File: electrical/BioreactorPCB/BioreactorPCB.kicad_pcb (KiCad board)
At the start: 2 copper layers, 90.7 x 84.9 mm, 90 parts, among them IC1 AL5809-20P1-7, IC2 VEML7700-TR, J1 61300311121, J10 USB_B, J11 Conn_01x06_Male, J12 Conn_02x03_Odd_Even, J13 PJ-202A, J14 Conn_01x05_Male, J15 Conn_01x06_Male, J16 Conn_01x06_Male, J2 61300311121, J3 Conn_01x05_Male, J4 Conn_01x06_Male, J5 OSTTC022162, J6 OSTTC022162, J7 OSTTC042162, J8 OSTTC042162, J9 OSTTC042162, Q1 2N3905, Q2 IRF540N, Q3 FQP47P06, Q4 TL2575HV-05IKV, U1 L293D, U2 FT232RL, U3 ATMEGA328P-AUR, U4 TCA39306DCUR, U5 ATmega328PB-M, Y1 16 mHz

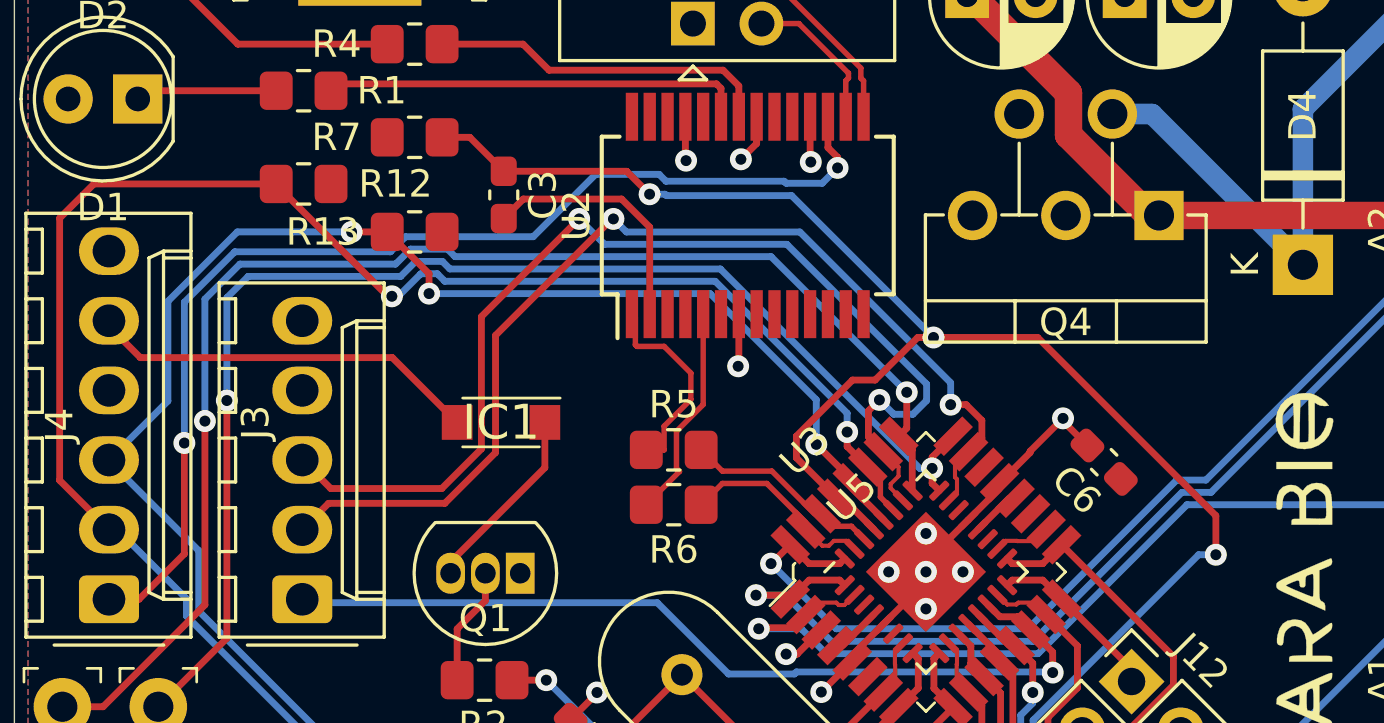
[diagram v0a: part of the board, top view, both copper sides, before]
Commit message: some track cleanup
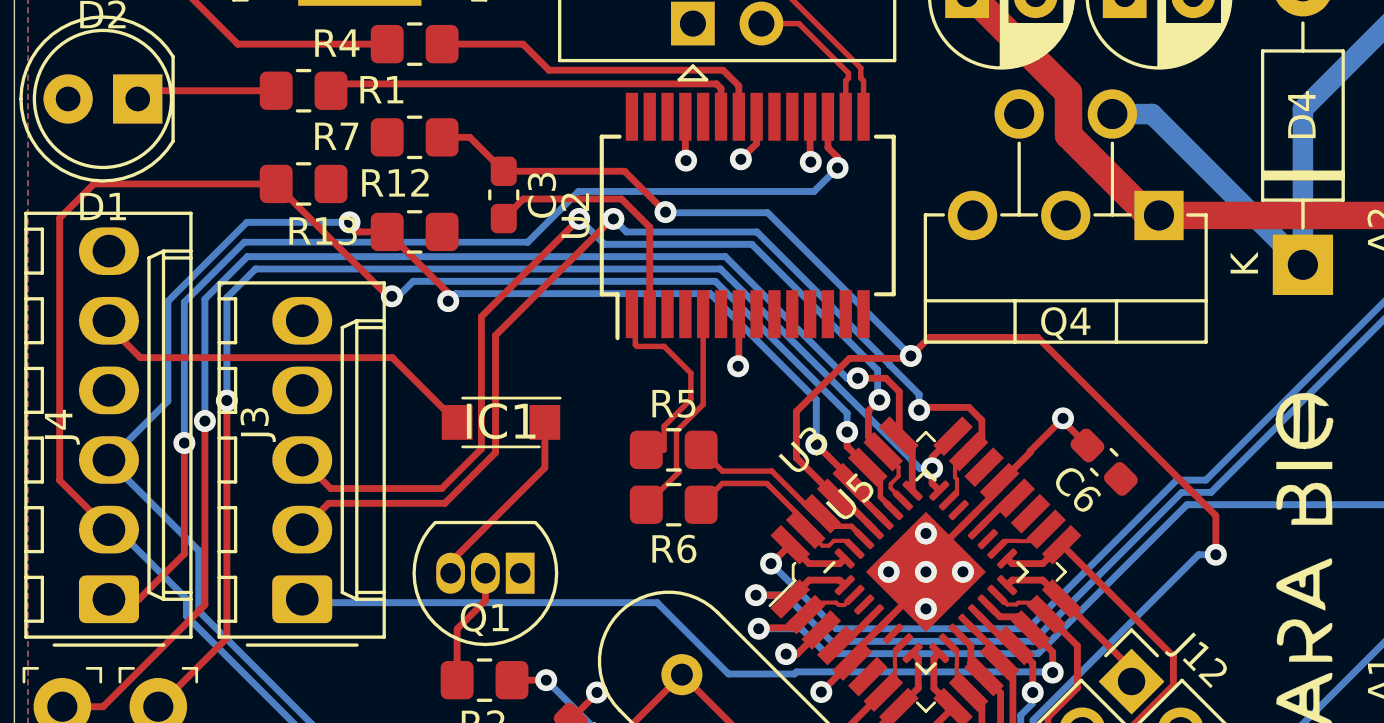
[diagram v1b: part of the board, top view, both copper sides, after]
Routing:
- net ROT_B: track 39.9 -> 36.3 mm
- net TEMP_OUT: track 50.3 -> 49.7 mm

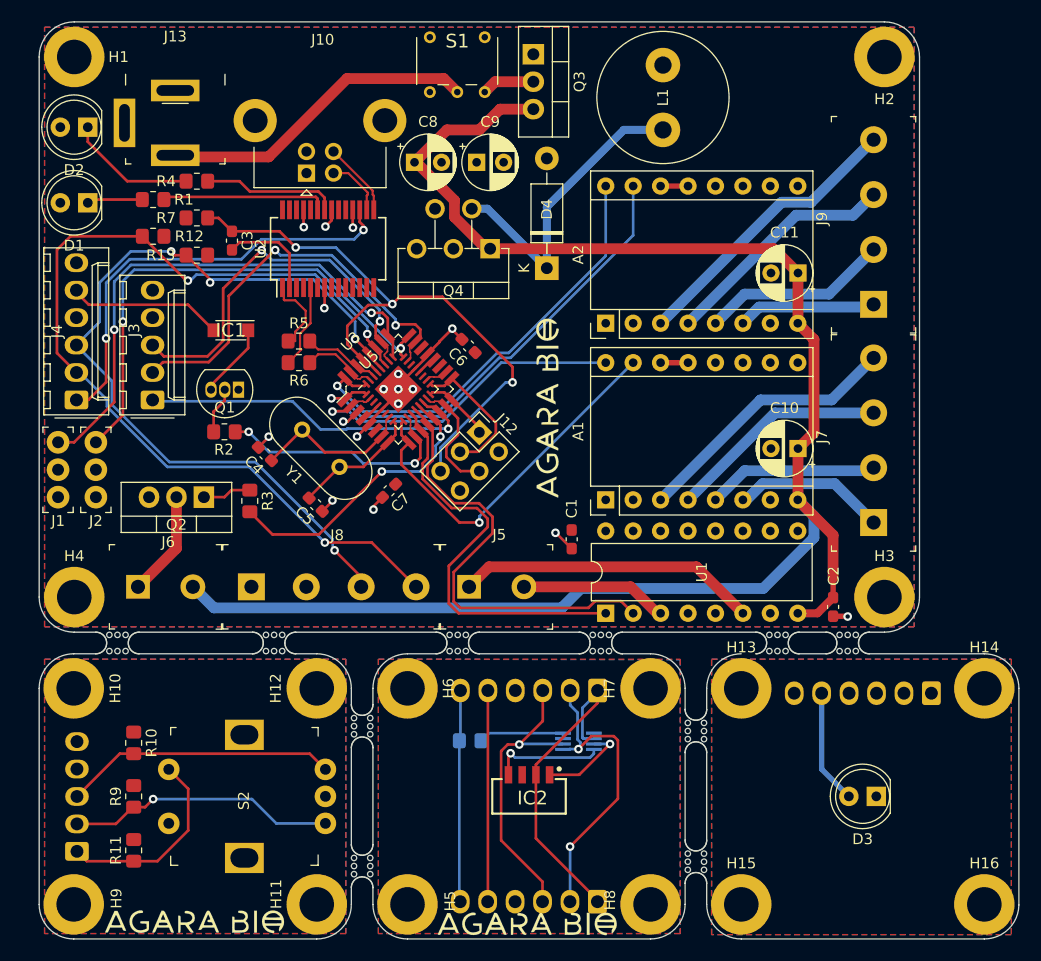
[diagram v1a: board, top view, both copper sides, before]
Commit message: many improvements to ground plane at some expense to 5V plane
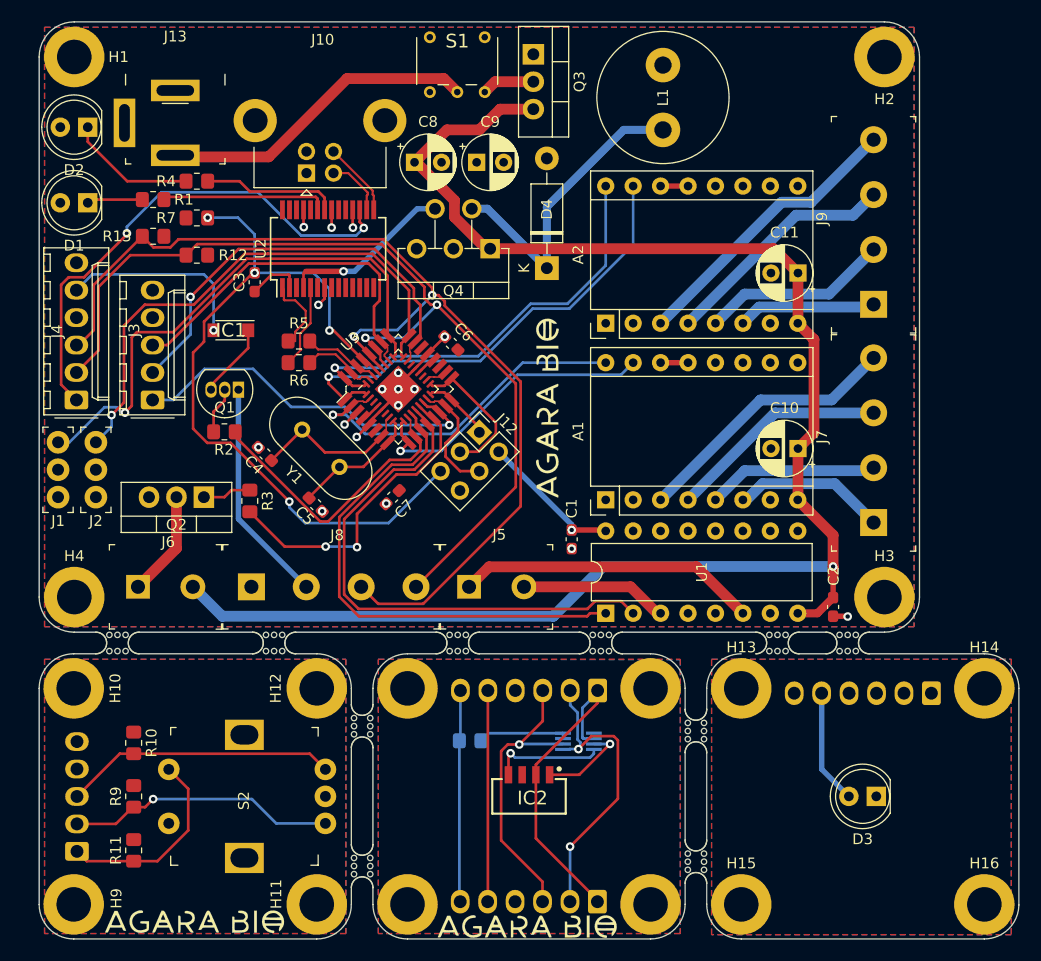
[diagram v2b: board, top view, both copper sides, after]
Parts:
- moved R12 4.41 mm to (96.3, 59.1)
- moved R13 4.41 mm to (92.3, 57.4)
- moved C3 4.39 mm to (101.7, 61.6)
- moved C6 1.61 mm to (119.9, 67.3)
- moved C7 0.68 mm to (114.5, 81.5)
- moved G*** 0.25 mm to (127.0, 121.2)
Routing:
- net +5V: track 4.69 -> 54.7 mm, vias 0 -> 2
- net SCL: track 76.7 -> 97.7 mm, vias 4 -> 2
- net RESET: track 57.9 -> 71.6 mm, vias 3 -> 4
- net GND: track 29.5 -> 20.6 mm
- net D7: track 38.7 -> 47.5 mm
- net D8: track 41.4 -> 50.2 mm
- net +3V3: track 40.5 -> 47.0 mm
- net D5: track 34.8 -> 28.4 mm
- net Net-(C3-Pad2): track 9.22 -> 5.03 mm
- net D6: track 22.2 -> 26.1 mm, vias 2 -> 0
- net Net-(IC1-Pad2): track 14.4 -> 18.0 mm, vias 0 -> 1
- net +12V: track 154.7 -> 151.9 mm, vias 0 -> 1
- net D9: track 26.6 -> 29.4 mm
- net ROT_B: track 36.3 -> 33.6 mm, vias 2 -> 0
- net BUTTON: track 32.2 -> 34.3 mm
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
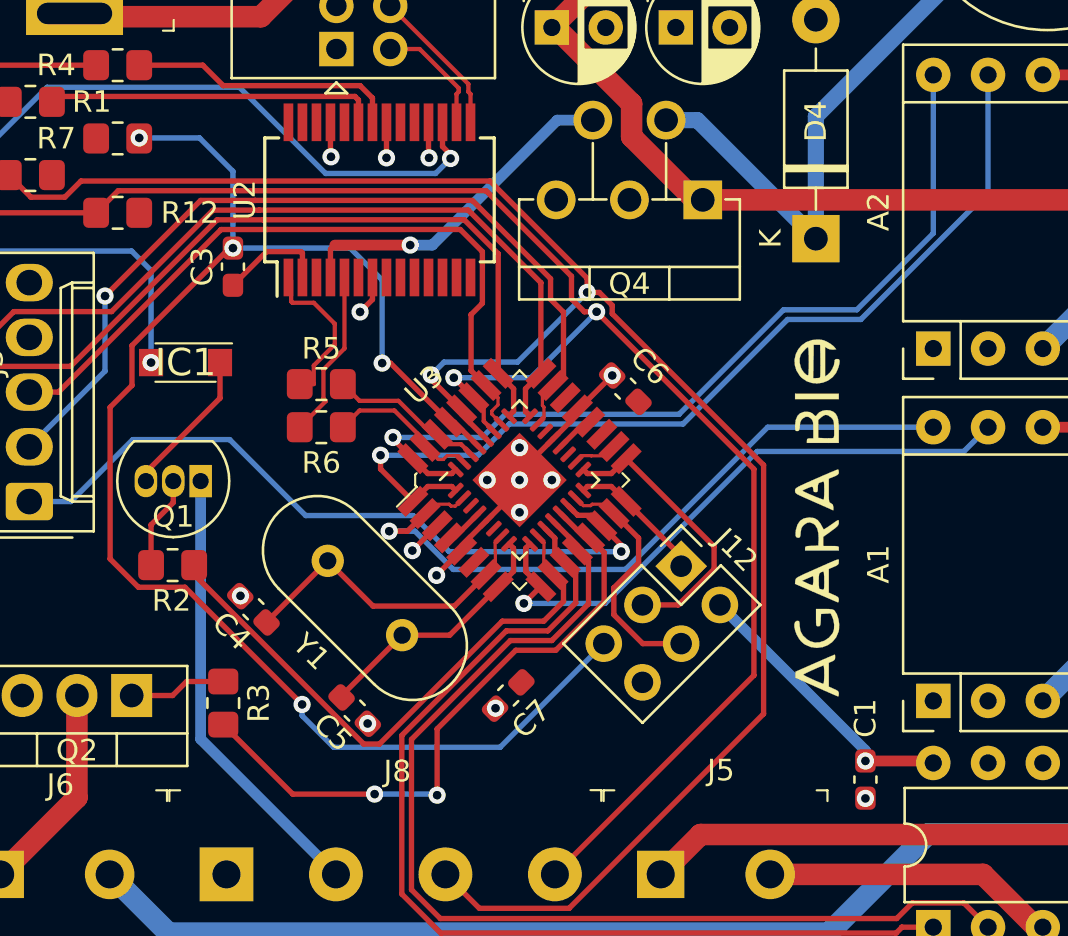
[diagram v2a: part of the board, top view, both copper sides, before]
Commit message: Removed vias in pad (so sad to see them go, but I'm  not made of money) and set min track width and spacing to 6 mil
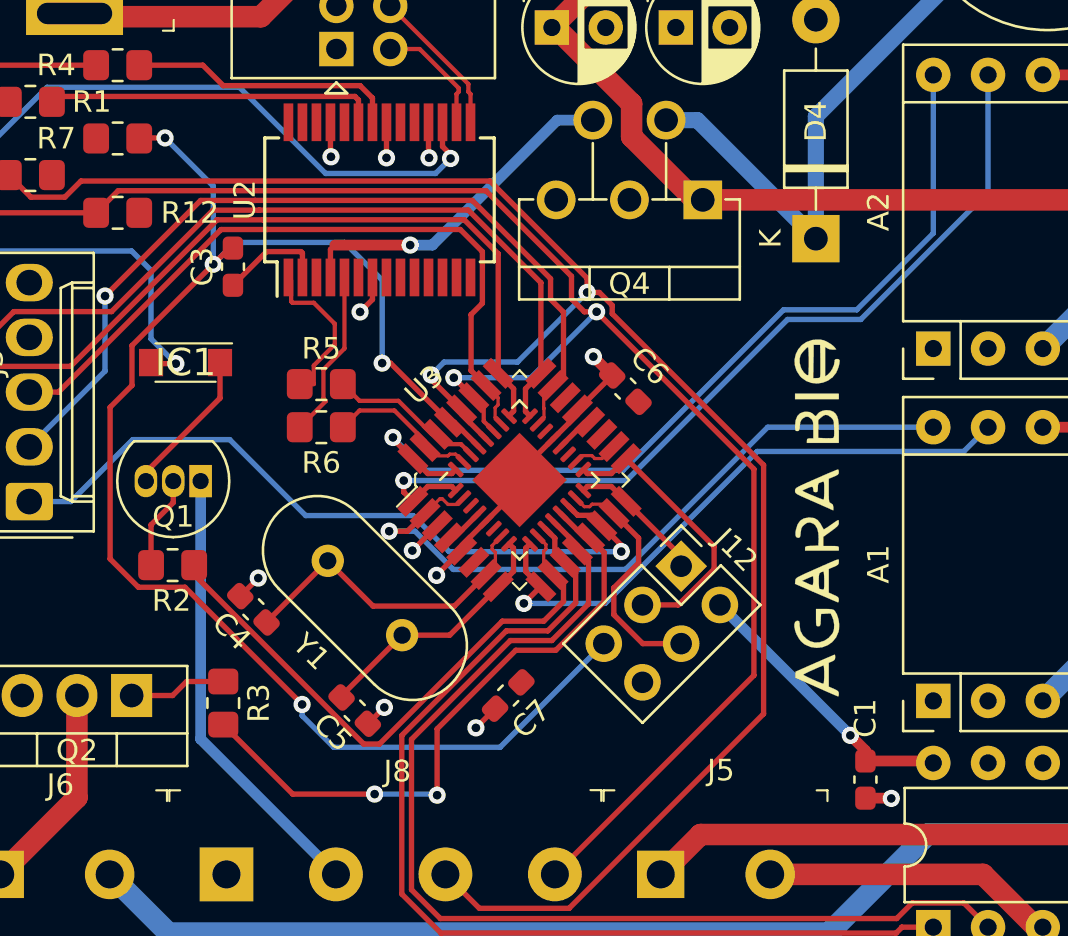
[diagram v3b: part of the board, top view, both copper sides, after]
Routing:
- net GND: track 20.6 -> 26.5 mm, vias 17 -> 12
- net D3: track 43.8 -> 41.6 mm
- net Net-(IC1-Pad2): track 18.0 -> 19.6 mm
- net D2: track 40.1 -> 41.3 mm
- net RESET: track 71.6 -> 72.4 mm
- net D4: track 31.6 -> 32.3 mm
- net XTAL+: track 14.3 -> 15.0 mm
- net D6: track 26.1 -> 26.8 mm
- net MOSI: track 10.8 -> 11.5 mm
- net +5V: track 54.7 -> 55.3 mm

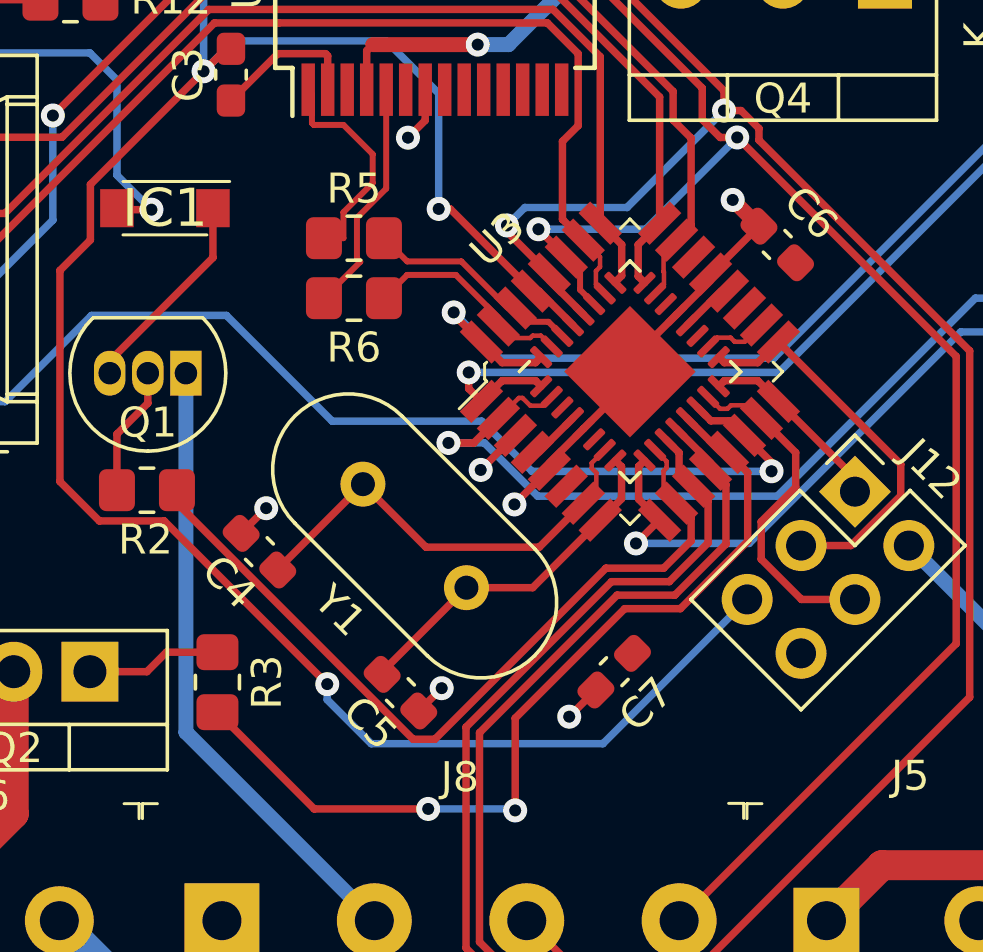
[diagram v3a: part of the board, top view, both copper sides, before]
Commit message: Replaced through-hole crystal with SMD package and moved capacitors so they actually decouple the MCU
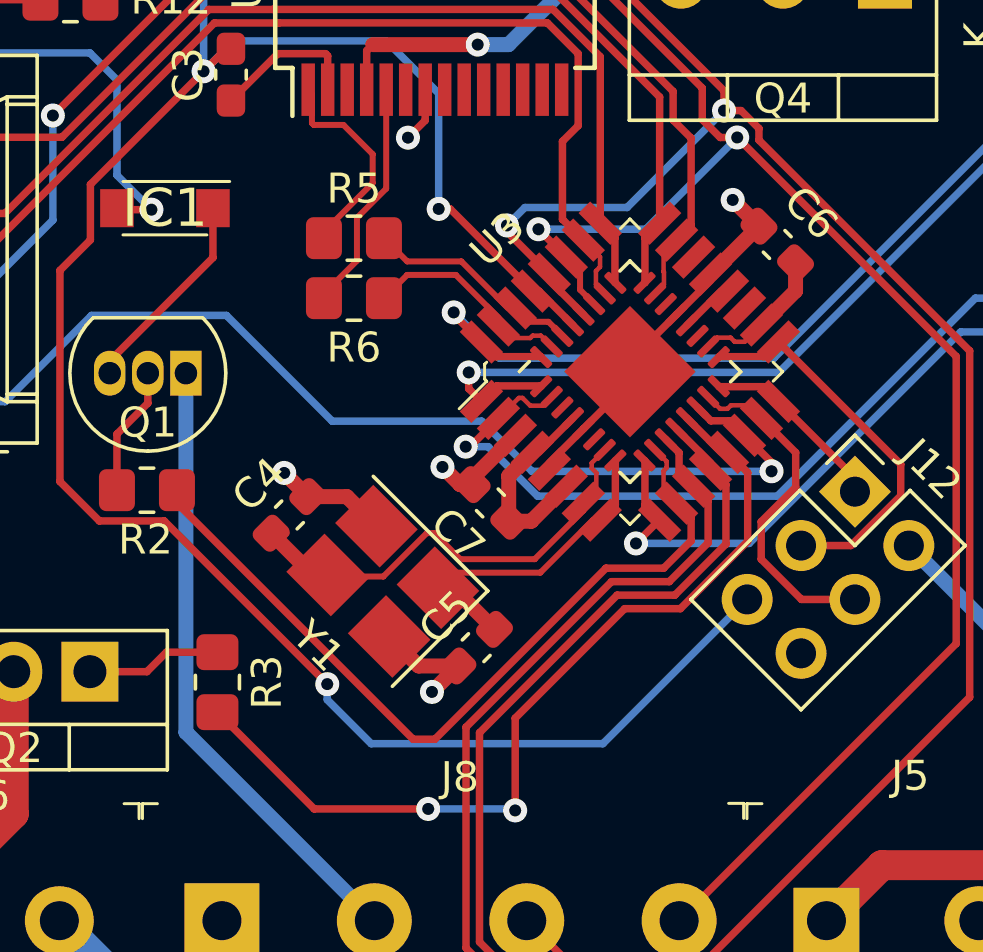
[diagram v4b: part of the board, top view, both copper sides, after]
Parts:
- Y1: footprint Crystal:Crystal_HC49-U_Vertical -> Crystal:Crystal_SMD_3225-4Pin_3.2x2.5mm_HandSoldering
- moved C7 6.98 mm to (110.3, 75.9), turned to -45 degrees
- moved C5 2.94 mm to (109.9, 80.7), turned to 45 degrees
- moved Y1 2.80 mm to (106.8, 78.5)
- moved C4 1.58 mm to (103.7, 76.3), turned to 45 degrees
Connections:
- Y1 pad 2: XTAL+ -> GND
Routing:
- net +5V: track 55.3 -> 62.9 mm
- net GND: track 26.5 -> 30.9 mm, vias 12 -> 10
- net D4: track 32.3 -> 31.2 mm
- net XTAL-: track 11.7 -> 11.1 mm
- net RX_TX_N: track 6.86 -> 6.25 mm
- net ROT_A: track 40.0 -> 39.3 mm
- net MOSI: track 11.5 -> 10.9 mm
- net D6: track 26.8 -> 26.1 mm
